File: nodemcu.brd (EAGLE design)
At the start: 47.9 x 48.2 mm, 8 parts

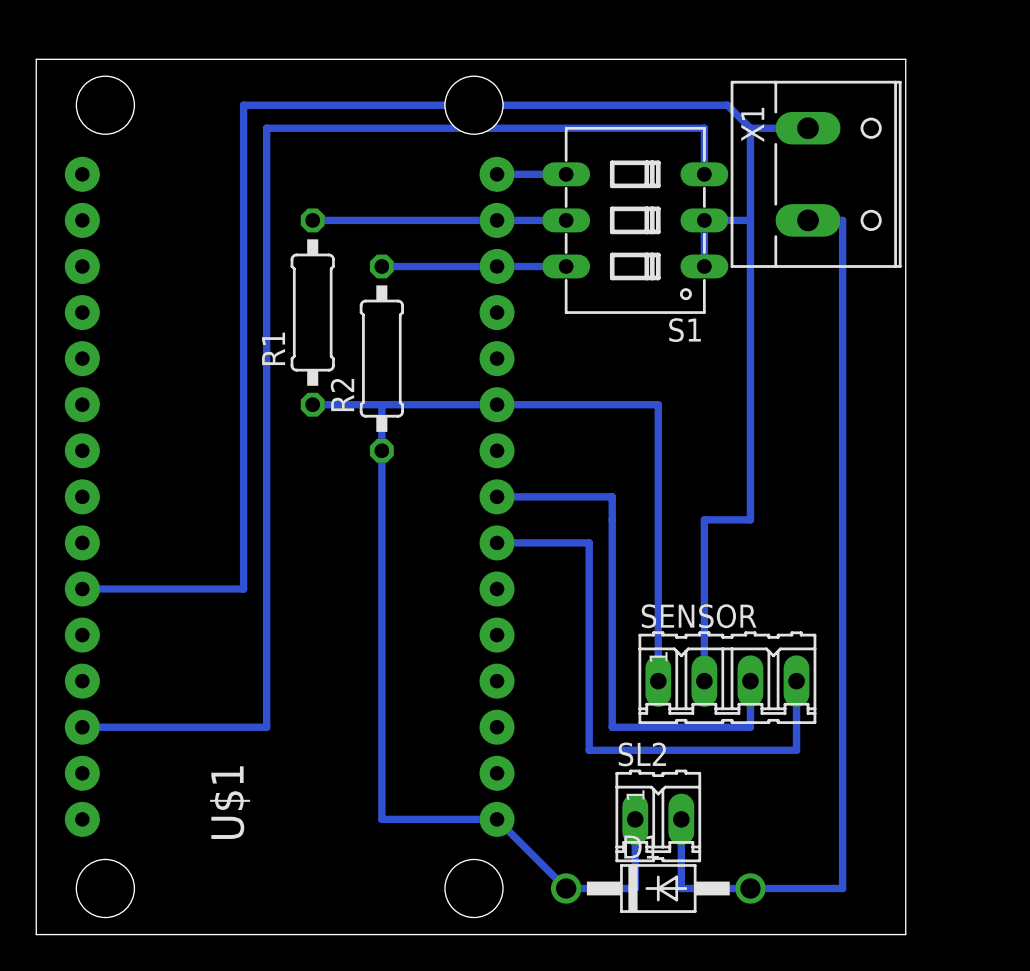
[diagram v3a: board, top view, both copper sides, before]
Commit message: změna tlouštky spojů
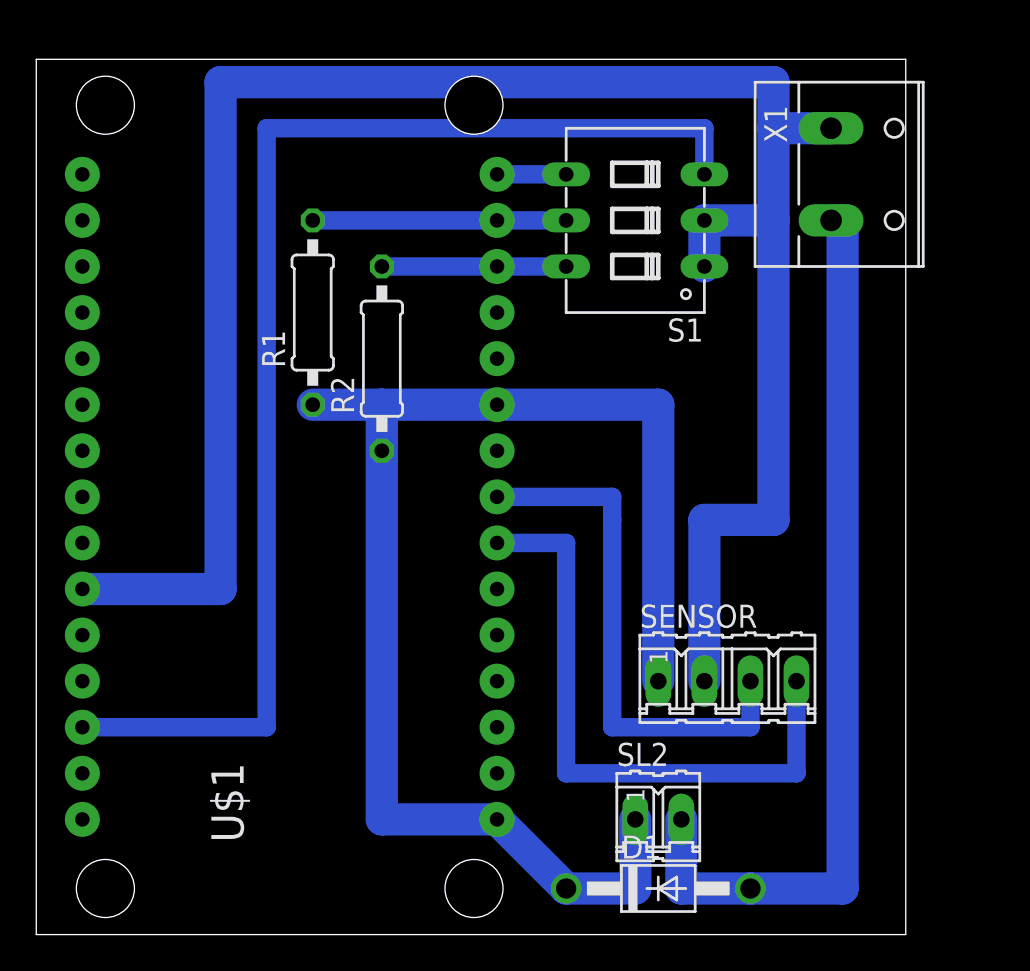
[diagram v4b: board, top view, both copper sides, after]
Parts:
- moved X1 1.27 mm to (44.5, 41.9)
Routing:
- net GND: track 105.3 -> 112.4 mm
- net N$2: track 31.7 -> 34.3 mm
- net N$5: track 51.4 -> 50.2 mm
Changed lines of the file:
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@@
 <wire x1="47.93" y1="48.25" x2="0" y2="48.25" width="0" layer="20"/>
 <wire x1="0" y1="48.25" x2="0" y2="0" width="0" layer="20"/>
-<dimension x1="0" y1="0" x2="0" y2="48.26" x3="-5.08" y3="24.13" textsize="1.778" layer="16"/>
-<dimension x1="0" y1="0" x2="47.93" y2="0" x3="23.965" y3="-6.35" textsize="1.778" layer="16"/>
 </plain>
 <attributes>
@@
 <attribute name="OC_NEWARK" value="unknown" x="38.1" y="13.97" size="1.778" layer="27" display="off"/>
 </element>
-<element name="X1" library="con-wago-508" package="W237-132" value="" x="43.18" y="41.91" rot="R270">
-<attribute name="OC_FARNELL" value="unknown" x="43.18" y="41.91" size="1.778" layer="27" rot="R270" display="off"/>
-<attribute name="MPN" value="" x="43.18" y="41.91" size="1.778" layer="27" rot="R270" display="off"/>
-<attribute name="MF" value="" x="43.18" y="41.91" size="1.778" layer="27" rot="R270" display="off"/>
-<attribute name="OC_NEWARK" value="unknown" x="43.18" y="41.91" size="1.778" layer="27" rot="R270" display="off"/>
+<element name="X1" library="con-wago-508" package="W237-132" value="" x="44.45" y="41.91" rot="R270">
+<attribute name="OC_FARNELL" value="unknown" x="44.45" y="41.91" size="1.778" layer="27" rot="R270" display="off"/>
+<attribute name="MPN" value="" x="44.45" y="41.91" size="1.778" layer="27" rot="R270" display="off"/>
+<attribute name="MF" value="" x="44.45" y="41.91" size="1.778" layer="27" rot="R270" display="off"/>
+<attribute name="OC_NEWARK" value="unknown" x="44.45" y="41.91" size="1.778" layer="27" rot="R270" display="off"/>
 </element>
 <element name="D1" library="diode" package="DO41-10" value="1N4004" x="34.29" y="2.54"/>
@@
 <contactref element="SL2" pad="1"/>
 <contactref element="U$1" pad="3V3@2"/>
-<wire x1="29.21" y1="2.54" x2="25.4" y2="6.35" width="0.4064" layer="16"/>
-<wire x1="29.21" y1="2.54" x2="33.02" y2="2.54" width="0.4064" layer="16"/>
-<wire x1="33.02" y1="2.54" x2="33.02" y2="6.35" width="0.4064" layer="16"/>
+<wire x1="29.21" y1="2.54" x2="25.4" y2="6.35" width="1.778" layer="16"/>
+<wire x1="29.21" y1="2.54" x2="33.02" y2="2.54" width="1.778" layer="16"/>
+<wire x1="33.02" y1="2.54" x2="33.02" y2="6.35" width="1.778" layer="16"/>
 <contactref element="R1" pad="1"/>
 <contactref element="R2" pad="1"/>
-<wire x1="19.05" y1="29.21" x2="15.24" y2="29.21" width="0.4064" layer="16"/>
-<wire x1="19.05" y1="26.67" x2="19.05" y2="29.21" width="0.4064" layer="16"/>
-<wire x1="34.29" y1="29.21" x2="34.29" y2="13.97" width="0.4064" layer="16"/>
+<wire x1="19.05" y1="29.21" x2="15.24" y2="29.21" width="1.778" layer="16"/>
+<wire x1="19.05" y1="26.67" x2="19.05" y2="29.21" width="1.778" layer="16"/>
+<wire x1="34.29" y1="29.21" x2="34.29" y2="13.97" width="1.778" layer="16"/>
 <contactref element="U$1" pad="3V3@1"/>
-<wire x1="19.05" y1="29.21" x2="25.4" y2="29.21" width="0.4064" layer="16"/>
-<wire x1="25.4" y1="29.21" x2="34.29" y2="29.21" width="0.4064" layer="16"/>
-<wire x1="25.4" y1="6.35" x2="19.05" y2="6.35" width="0.4064" layer="16"/>
-<wire x1="19.05" y1="6.35" x2="19.05" y2="26.67" width="0.4064" layer="16"/>
+<wire x1="19.05" y1="29.21" x2="25.4" y2="29.21" width="1.778" layer="16"/>
+<wire x1="25.4" y1="29.21" x2="34.29" y2="29.21" width="1.778" layer="16"/>
+<wire x1="25.4" y1="6.35" x2="19.05" y2="6.35" width="1.778" layer="16"/>
+<wire x1="19.05" y1="6.35" x2="19.05" y2="26.67" width="1.778" layer="16"/>
 </signal>
 <signal name="GND">
 <contactref element="SENSOR" pad="2"/>
 <contactref element="X1" pad="1"/>
-<wire x1="42.545" y1="44.45" x2="39.37" y2="44.45" width="0.4064" layer="16"/>
-<wire x1="39.37" y1="44.45" x2="39.37" y2="39.37" width="0.4064" layer="16"/>
-<wire x1="39.37" y1="39.37" x2="39.37" y2="22.86" width="0.4064" layer="16"/>
-<wire x1="39.37" y1="22.86" x2="36.83" y2="22.86" width="0.4064" layer="16"/>
-<wire x1="36.83" y1="22.86" x2="36.83" y2="13.97" width="0.4064" layer="16"/>
+<wire x1="43.815" y1="44.45" x2="40.64" y2="44.45" width="1.778" layer="16"/>
+<wire x1="40.64" y1="44.45" x2="40.64" y2="39.37" width="1.778" layer="16"/>
+<wire x1="40.64" y1="39.37" x2="40.64" y2="22.86" width="1.778" layer="16"/>
+<wire x1="40.64" y1="22.86" x2="36.83" y2="22.86" width="1.778" layer="16"/>
+<wire x1="36.83" y1="22.86" x2="36.83" y2="13.97" width="1.778" layer="16"/>
 <contactref element="U$1" pad="GND@0"/>
-<wire x1="2.54" y1="19.05" x2="11.43" y2="19.05" width="0.4064" layer="16"/>
-<wire x1="11.43" y1="19.05" x2="11.43" y2="45.72" width="0.4064" layer="16"/>
-<wire x1="11.43" y1="45.72" x2="38.1" y2="45.72" width="0.4064" layer="16"/>
-<wire x1="38.1" y1="45.72" x2="39.37" y2="44.45" width="0.4064" layer="16"/>
+<wire x1="2.54" y1="19.05" x2="10.16" y2="19.05" width="1.778" layer="16"/>
+<wire x1="10.16" y1="19.05" x2="10.16" y2="46.99" width="1.778" layer="16"/>
+<wire x1="10.16" y1="46.99" x2="40.64" y2="46.99" width="1.778" layer="16"/>
+<wire x1="40.64" y1="46.99" x2="40.64" y2="44.45" width="1.778" layer="16"/>
 <contactref element="S1" pad="1"/>
 <contactref element="S1" pad="2"/>
-<wire x1="36.83" y1="36.83" x2="36.83" y2="39.37" width="0.4064" layer="16"/>
-<wire x1="36.83" y1="39.37" x2="39.37" y2="39.37" width="0.4064" layer="16"/>
+<wire x1="36.83" y1="36.83" x2="36.83" y2="39.37" width="1.778" layer="16"/>
+<wire x1="36.83" y1="39.37" x2="40.64" y2="39.37" width="1.778" layer="16"/>
 </signal>
 <signal name="N$1">
 <contactref element="U$1" pad="D0"/>
 <contactref element="S1" pad="4"/>
-<wire x1="25.4" y1="41.91" x2="29.21" y2="41.91" width="0.4064" layer="16"/>
+<wire x1="25.4" y1="41.91" x2="29.21" y2="41.91" width="1.016" layer="16"/>
 </signal>
 <signal name="N$2">
 <contactref element="SENSOR" pad="4"/>
 <contactref element="U$1" pad="D6"/>
-<wire x1="41.91" y1="13.97" x2="41.91" y2="10.16" width="0.4064" layer="16"/>
-<wire x1="41.91" y1="10.16" x2="30.48" y2="10.16" width="0.4064" layer="16"/>
-<wire x1="30.48" y1="10.16" x2="30.48" y2="21.59" width="0.4064" layer="16"/>
-<wire x1="30.48" y1="21.59" x2="25.4" y2="21.59" width="0.4064" layer="16"/>
+<wire x1="41.91" y1="13.97" x2="41.91" y2="8.89" width="1.016" layer="16"/>
+<wire x1="41.91" y1="8.89" x2="29.21" y2="8.89" width="1.016" layer="16"/>
+<wire x1="29.21" y1="8.89" x2="29.21" y2="21.59" width="1.016" layer="16"/>
+<wire x1="29.21" y1="21.59" x2="25.4" y2="21.59" width="1.016" layer="16"/>
 </signal>
 <signal name="N$3">
 <contactref element="U$1" pad="D5"/>
 <contactref element="SENSOR" pad="3"/>
-<wire x1="39.37" y1="13.97" x2="39.37" y2="11.43" width="0.4064" layer="16"/>
-<wire x1="39.37" y1="11.43" x2="31.75" y2="11.43" width="0.4064" layer="16"/>
-<wire x1="31.75" y1="11.43" x2="31.75" y2="22.86" width="0.4064" layer="16"/>
-<wire x1="31.75" y1="22.86" x2="31.75" y2="24.13" width="0.4064" layer="16"/>
-<wire x1="31.75" y1="24.13" x2="25.4" y2="24.13" width="0.4064" layer="16"/>
+<wire x1="39.37" y1="13.97" x2="39.37" y2="11.43" width="1.016" layer="16"/>
+<wire x1="39.37" y1="11.43" x2="31.75" y2="11.43" width="1.016" layer="16"/>
+<wire x1="31.75" y1="11.43" x2="31.75" y2="22.86" width="1.016" layer="16"/>
+<wire x1="31.75" y1="22.86" x2="31.75" y2="24.13" width="1.016" layer="16"/>
+<wire x1="31.75" y1="24.13" x2="25.4" y2="24.13" width="1.016" layer="16"/>
 </signal>
 <signal name="N$4">
 <contactref element="U$1" pad="RST"/>
-<wire x1="2.54" y1="11.43" x2="12.7" y2="11.43" width="0.4064" layer="16"/>
-<wire x1="12.7" y1="44.45" x2="12.7" y2="11.43" width="0.4064" layer="16"/>
+<wire x1="2.54" y1="11.43" x2="12.7" y2="11.43" width="1.016" layer="16"/>
+<wire x1="12.7" y1="44.45" x2="12.7" y2="11.43" width="1.016" layer="16"/>
 <contactref element="S1" pad="3"/>
-<wire x1="12.7" y1="44.45" x2="36.83" y2="44.45" width="0.4064" layer="16"/>
-<wire x1="36.83" y1="44.45" x2="36.83" y2="41.91" width="0.4064" layer="16"/>
+<wire x1="12.7" y1="44.45" x2="36.83" y2="44.45" width="1.016" layer="16"/>
+<wire x1="36.83" y1="44.45" x2="36.83" y2="41.91" width="1.016" layer="16"/>
 </signal>
 <signal name="N$5">
@@
 <contactref element="D1" pad="A"/>
 <contactref element="SL2" pad="2"/>
-<wire x1="42.545" y1="39.37" x2="44.45" y2="39.37" width="0.4064" layer="16"/>
-<wire x1="44.45" y1="39.37" x2="44.45" y2="2.54" width="0.4064" layer="16"/>
-<wire x1="39.37" y1="2.54" x2="44.45" y2="2.54" width="0.4064" layer="16"/>
-<wire x1="35.56" y1="6.35" x2="35.56" y2="2.54" width="0.4064" layer="16"/>
-<wire x1="35.56" y1="2.54" x2="39.37" y2="2.54" width="0.4064" layer="16"/>
+<wire x1="43.815" y1="39.37" x2="44.45" y2="39.37" width="1.778" layer="16"/>
+<wire x1="44.45" y1="39.37" x2="44.45" y2="2.54" width="1.778" layer="16"/>
+<wire x1="39.37" y1="2.54" x2="44.45" y2="2.54" width="1.778" layer="16"/>
+<wire x1="35.56" y1="6.35" x2="35.56" y2="2.54" width="1.778" layer="16"/>
+<wire x1="35.56" y1="2.54" x2="39.37" y2="2.54" width="1.778" layer="16"/>
 </signal>
 <signal name="N$8">
@@
 <contactref element="S1" pad="5"/>
 <contactref element="R1" pad="2"/>
-<wire x1="25.4" y1="39.37" x2="15.24" y2="39.37" width="0.4064" layer="16"/>
-<wire x1="25.4" y1="39.37" x2="29.21" y2="39.37" width="0.4064" layer="16"/>
+<wire x1="25.4" y1="39.37" x2="15.24" y2="39.37" width="1.016" layer="16"/>
+<wire x1="25.4" y1="39.37" x2="29.21" y2="39.37" width="1.016" layer="16"/>
 </signal>
 <signal name="N$9">
@@
 <contactref element="S1" pad="6"/>
 <contactref element="R2" pad="2"/>
-<wire x1="25.4" y1="36.83" x2="19.05" y2="36.83" width="0.4064" layer="16"/>
-<wire x1="25.4" y1="36.83" x2="29.21" y2="36.83" width="0.4064" layer="16"/>
+<wire x1="25.4" y1="36.83" x2="19.05" y2="36.83" width="1.016" layer="16"/>
+<wire x1="25.4" y1="36.83" x2="29.21" y2="36.83" width="1.016" layer="16"/>
 </signal>
 </signals>

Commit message: uprava desky
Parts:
- moved S1 5.08 mm to (38.1, 39.4)
- moved D1 3.81 mm to (38.1, 2.54)
- moved SL2 3.81 mm to (38.1, 6.35)
- moved U$1 3.81 mm to (17.8, 24.1)
- moved X1 3.81 mm to (48.3, 41.9)
- moved SENSOR 2.54 mm to (40.6, 14.0)
- moved R1 1.27 mm to (16.5, 34.3)
- moved R2 1.27 mm to (20.3, 31.8)
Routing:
- net N$4: track 69.9 -> 76.2 mm
- net GND: track 112.4 -> 117.5 mm
- net N$9: track 10.2 -> 14.0 mm
- net N$8: track 14.0 -> 17.8 mm
- net +3V3: track 76.5 -> 78.1 mm
- net N$3: track 29.2 -> 27.9 mm
- net N$2: track 34.3 -> 33.0 mm
- net N$1: track 3.81 -> 5.08 mm
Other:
- board size 47.9 x 48.2 mm -> 51.7 x 48.2 mm
